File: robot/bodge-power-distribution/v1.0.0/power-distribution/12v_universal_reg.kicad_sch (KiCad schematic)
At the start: 23 parts

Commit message: Incomplete bodge-power-distribution schematics
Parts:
- added F?: TBD_LOGIC_FUSE, symbol Device:Fuse
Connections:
- net PGOOD_{OD} renamed PGOOD
- net V_FB_12v0: no longer names the net of R?.1, R?.2, U?.5 (V_{FB})
- net Vbatt_6s: no longer names the net of C?.1, C?.1, C?.1, C?.1, R?.1, R?.1, R?.2, U?.11 (V_{IN})
- net Vbatt_6s: now also F?.2
- new net V_{BATT(6S)}: F?.1
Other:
- title: Motorboard -> Power Distribution
- moved on the sheet: C?, D?, L?, Q?, R?, U?

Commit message: Incomplete bodge-power-distribution schematics
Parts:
- gave numbers to parts that had none: 24
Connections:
- net V_{BATT(6S)} renamed V_{IN}

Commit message: Sync
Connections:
- net PGOOD renamed PGOOD_{12v0}
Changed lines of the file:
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@@
     (effects (font (size 1.27 1.27)) (justify left bottom))
   )
-  (label "PGOOD" (at 39.37 38.1 0)
+  (label "PGOOD_{12v0}" (at 39.37 38.1 0)
     (effects (font (size 1.27 1.27)) (justify left bottom))
   )
-  (label "PGOOD" (at 44.45 102.87 180)
+  (label "PGOOD_{12v0}" (at 44.45 102.87 180)
     (effects (font (size 1.27 1.27)) (justify right bottom))
   )
@@
     (effects (font (size 1.27 1.27)) (justify right bottom))
   )
-  (hierarchical_label "PGOOD" (shape output) (at 35.56 38.1 180)
+  (hierarchical_label "PGOOD_{12v0}" (shape output) (at 35.56 38.1 180)
     (effects (font (size 1.27 1.27)) (justify right))
   )

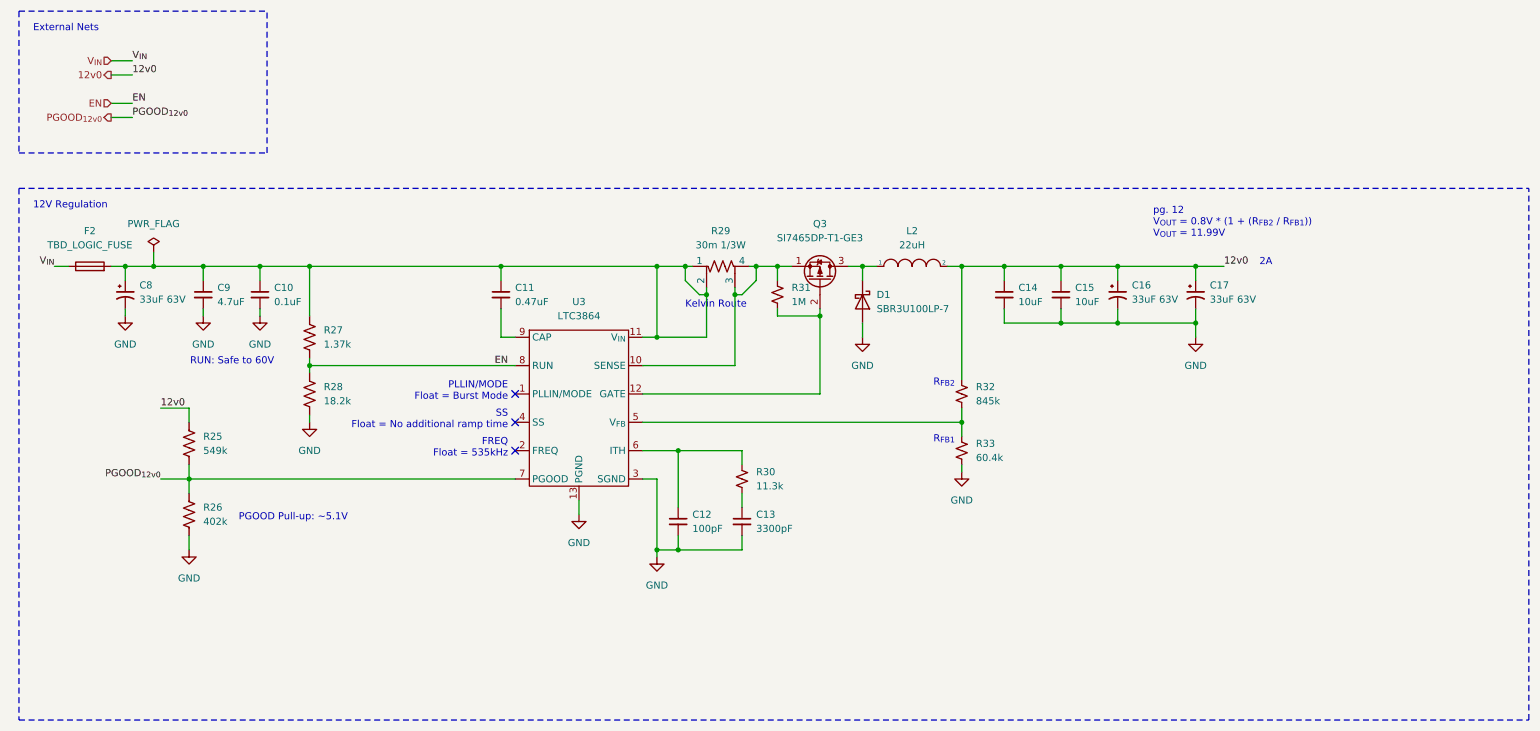
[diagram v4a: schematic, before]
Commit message: Rename transistors library to AT-Transistors
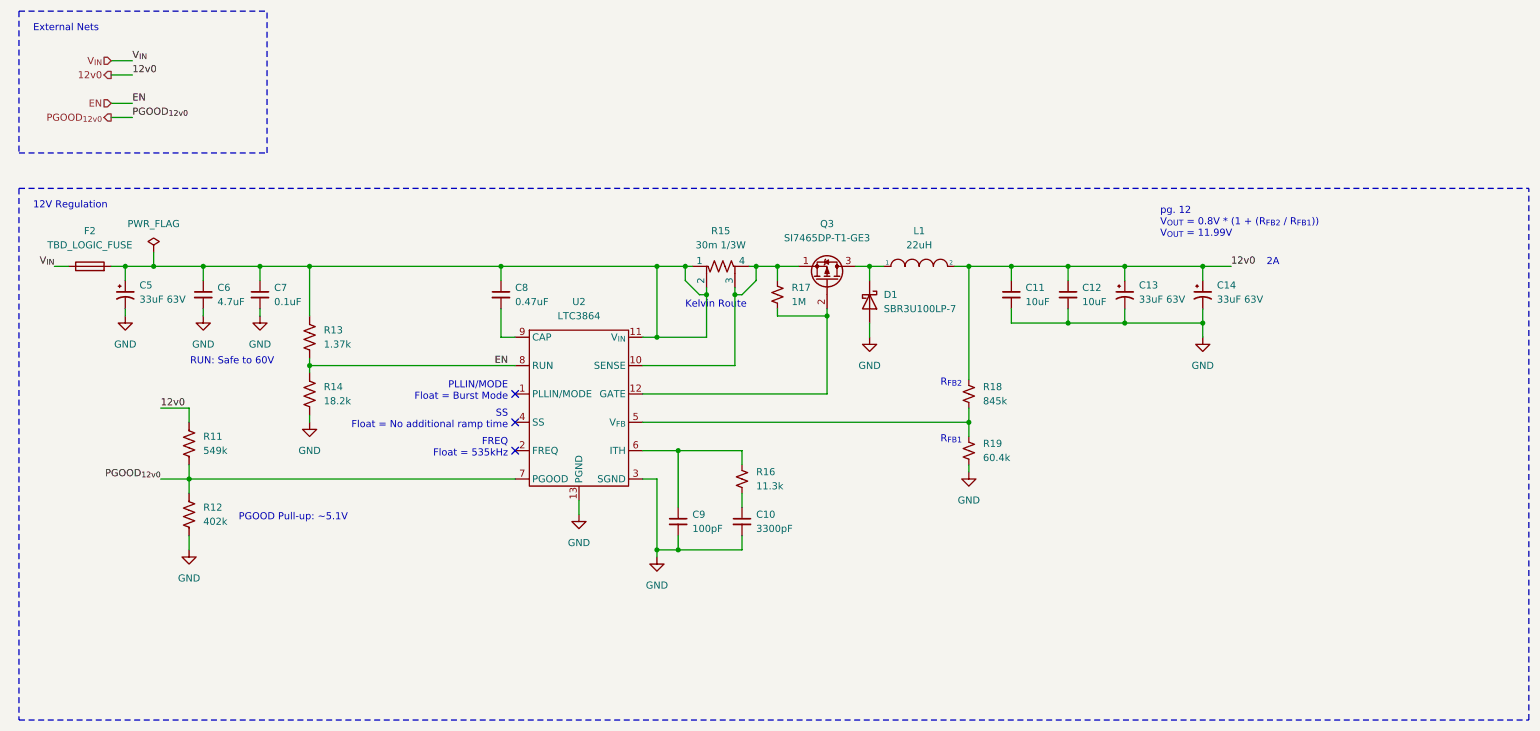
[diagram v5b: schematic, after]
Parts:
- renumbered C13 to C10, C14 to C11, C15 to C12, C16 to C13, C17 to C14, C8 to C5, C9 to C6, C10 to C7, C11 to C8, C12 to C9, L2 to L1, R25 to R11, R26 to R12, R27 to R13, R28 to R14, R29 to R15, R30 to R16, R31 to R17, R32 to R18, R33 to R19, U3 to U2
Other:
- moved on the sheet: C11, C12, C13, C14, D1, L1, Q3, R18, R19

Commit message: Component updates
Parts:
- removed Q3: SI7465DP-T1-GE3, Package_TO_SOT_SMD:Vishay_PowerPAK_SC70-6L_Single, symbol Device:Q_PMOS_SGD
- added Q3: SI7465DP-T1-GE3, Package_SO:PowerPAK_SO-8_Single, symbol AT-Transistors:Q_PMOS_SGD_PowerPAK
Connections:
- net at D1.1 (K), L1.1: now also Q3.5 (D)
- net at R15.3, R15.4, R17.1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: now also Q3.1 (S), Q3.2 (S), Q3.3 (S)
- net at R17.2, U2.12 (GATE): now also Q3.4 (G)
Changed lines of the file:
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@@
   (junction (at 154.94 64.77) (diameter 0) (color 0 0 0 0)
+  )
+  (junction (at 154.94 62.23) (diameter 0) (color 0 0 0 0)
   )
   (junction (at 207.01 74.93) (diameter 0) (color 0 0 0 0)
@@
     (stroke (width 0) (type solid) (color 0 0 0 0))
   )
+  (wire (pts (xy 158.75 59.69) (xy 154.94 59.69))
+    (stroke (width 0) (type default) (color 0 0 0 0))
+  )
   (wire (pts (xy 168.91 64.77) (xy 171.45 64.77))
     (stroke (width 0) (type default) (color 0 0 0 0))
@@
     (stroke (width 0) (type default) (color 0 0 0 0))
   )
+  (wire (pts (xy 154.94 62.23) (xy 154.94 64.77))
+    (stroke (width 0) (type default) (color 0 0 0 0))
+  )
   (wire (pts (xy 25.4 64.77) (xy 27.94 64.77))
     (stroke (width 0) (type solid) (color 0 0 0 0))
@@
     (stroke (width 0) (type default) (color 0 0 0 0))
   )
+  (wire (pts (xy 154.94 59.69) (xy 154.94 62.23))
+    (stroke (width 0) (type default) (color 0 0 0 0))
+  )
   (wire (pts (xy 189.23 64.77) (xy 189.23 85.09))
+    (stroke (width 0) (type default) (color 0 0 0 0))
+  )
+  (wire (pts (xy 154.94 62.23) (xy 158.75 62.23))
     (stroke (width 0) (type default) (color 0 0 0 0))
   )
@@
     (pin "1")
   )
+  (symbol (lib_id "AT-Transistors:Q_PMOS_SGD_PowerPAK") (at 163.83 67.31 270) (mirror x) (unit 1)
+    (in_bom yes) (on_board yes) (fields_autoplaced)
+    (property "Reference" "Q3" (id 0) (at 163.83 54.61 90))
+    (property "Value" "SI7465DP-T1-GE3" (id 1) (at 163.83 57.15 90))
+    (property "Footprint" "Package_SO:PowerPAK_SO-8_Single" (id 2) (at 166.37 62.23 0)
+      (effects (font (size 1.27 1.27)) hide)
+    )
+    (property "Datasheet" "~" (id 3) (at 163.83 67.31 0)
+      (effects (font (size 1.27 1.27)) hide)
+    )
+    (pin "1")
+    (pin "2")
+    (pin "3")
+    (pin "4")
+    (pin "5")
+  )
   (symbol (lib_id "power:GND") (at 189.23 101.6 0) (unit 1)
     (in_bom yes) (on_board yes) (fields_autoplaced)
@@
     (pin "2")
   )
-  (symbol (lib_id "Device:Q_PMOS_SGD") (at 163.83 67.31 270) (mirror x) (unit 1)
-    (in_bom yes) (on_board yes) (fields_autoplaced)
-    (property "Reference" "Q3" (id 0) (at 163.83 57.15 90))
-    (property "Value" "SI7465DP-T1-GE3" (id 1) (at 163.83 59.69 90))
-    (property "Footprint" "Package_TO_SOT_SMD:Vishay_PowerPAK_SC70-6L_Single" (id 2) (at 166.37 62.23 0)
-      (effects (font (size 1.27 1.27)) hide)
-    )
-    (property "Datasheet" "~" (id 3) (at 163.83 67.31 0)
-      (effects (font (size 1.27 1.27)) hide)
-    )
-    (pin "1")
-    (pin "2")
-    (pin "3")
-  )
   (symbol (lib_id "power:GND") (at 171.45 77.47 0) (unit 1)
